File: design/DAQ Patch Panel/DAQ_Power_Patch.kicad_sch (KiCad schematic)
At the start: 18 parts, among them J1 Power 1 Terminal, J2 Screw_Terminal_01x06, J3 Power 2 Terminal, J4 12-Pole-PCB-Triple-Layer-Conn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, J7 Sensor 1 Terminal

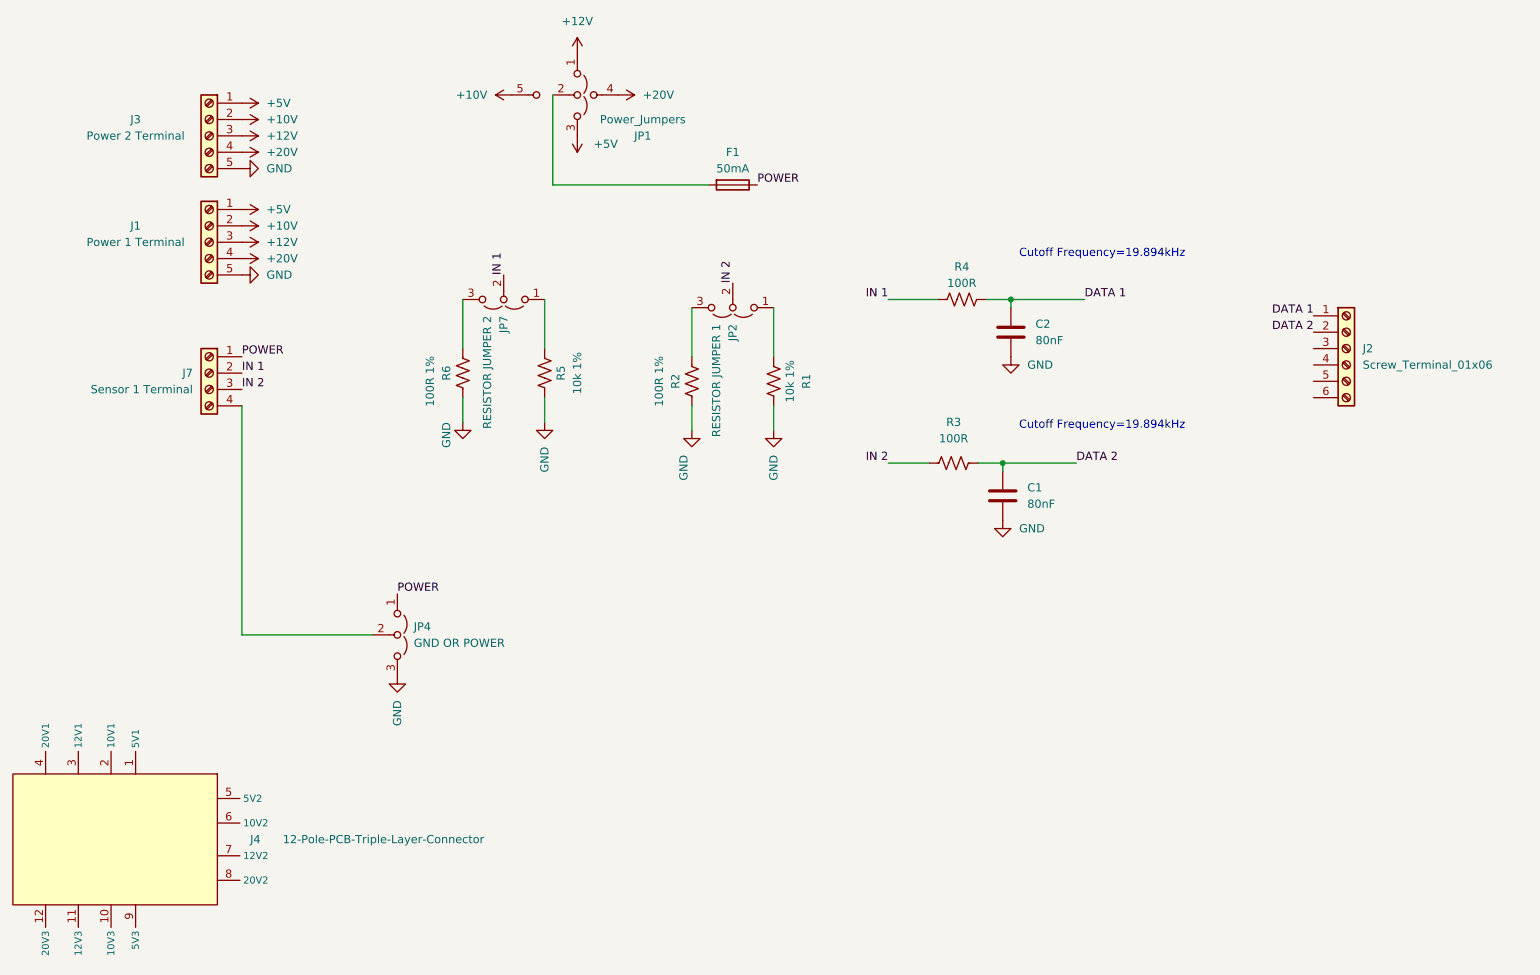
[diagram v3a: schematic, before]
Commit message: Hierarchecal Sheets Added and Sensor Ports Triplicated
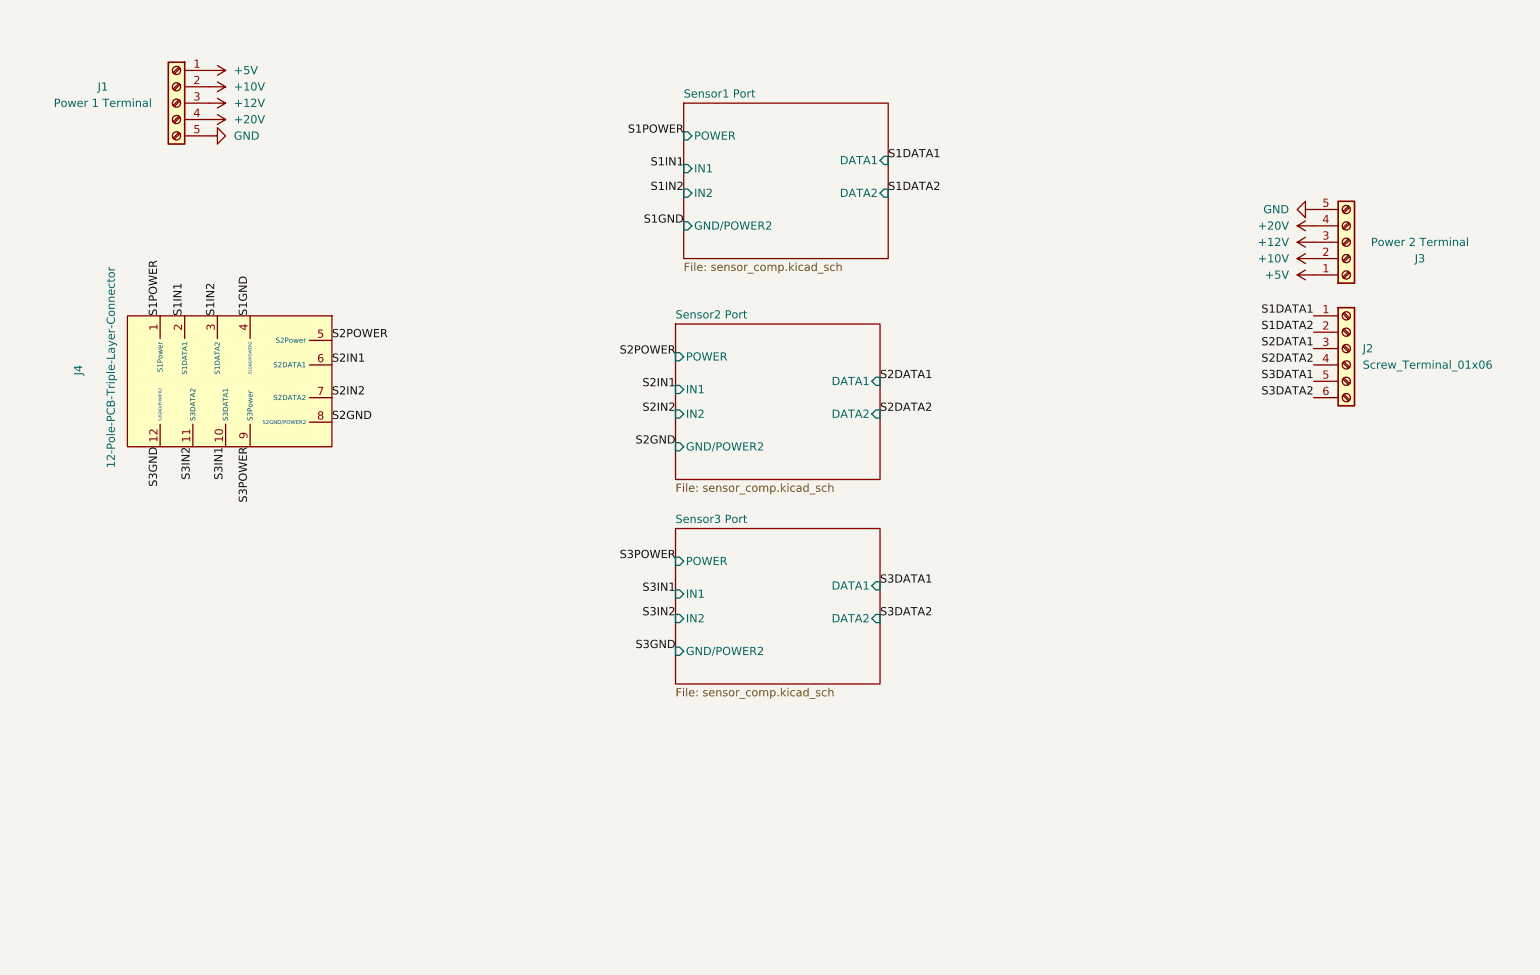
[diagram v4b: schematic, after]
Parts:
- removed C1, C2: 80nF, Capacitor_SMD:C_0805_2012Metric_Pad1.18x1.45mm_HandSolder, symbol Device:C
- removed F1: 50mA, Fuse:Fuse_0805_2012Metric_Pad1.15x1.40mm_HandSolder, symbol Device:Fuse
- removed J7: Sensor 1 Terminal, TerminalBlock_Phoenix:TerminalBlock_Phoenix_MKDS-1,5-4-5.08_1x04_P5.08mm_Horizontal, symbol Connector:Screw_Terminal_01x04
- removed JP1: Power_Jumpers, Library:4-Pole Jumper, symbol Jumper:Jumper_3_Open
- removed JP2: RESISTOR JUMPER 1, Connector_PinHeader_2.54mm:PinHeader_1x03_P2.54mm_Vertical, symbol Jumper:Jumper_3_Open
- removed JP4: GND OR POWER, Connector_PinHeader_2.54mm:PinHeader_1x03_P2.54mm_Vertical, symbol Jumper:Jumper_3_Open
- removed JP7: RESISTOR JUMPER 2, Connector_PinHeader_2.54mm:PinHeader_1x03_P2.54mm_Vertical, symbol Jumper:Jumper_3_Open
- removed R1, R5: 10k 1%, Resistor_SMD:R_0805_2012Metric_Pad1.20x1.40mm_HandSolder, symbol Device:R_US
- removed R2, R6: 100R 1%, Resistor_SMD:R_0805_2012Metric_Pad1.20x1.40mm_HandSolder, symbol Device:R_US
- removed R3, R4: 100R, Resistor_SMD:R_0805_2012Metric_Pad1.20x1.40mm_HandSolder, symbol Device:R_US
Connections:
- net S2DATA1: now reaches J2.3 (Pin_3)
- net S2DATA2: now reaches J2.4 (Pin_4)
- net S3DATA1: now reaches J2.5 (Pin_5)
- net S3DATA2: now reaches J2.6 (Pin_6)
- net S1POWER: now reaches J4.1 (S1Power)
- net S3IN1: now reaches J4.10 (S3DATA1)
- net S3IN2: now reaches J4.11 (S3DATA2)
- net S3GND: now reaches J4.12 (S3GND/POWER2)
- net S1IN1: now reaches J4.2 (S1DATA1)
- net S1IN2: now reaches J4.3 (S1DATA2)
- net S1GND: now reaches J4.4 (S1GND/POWER2)
- net S2POWER: now reaches J4.5 (S2Power)
- net S2IN1: now reaches J4.6 (S2DATA1)
- net S2IN2: now reaches J4.7 (S2DATA2)
- net S2GND: now reaches J4.8 (S2GND/POWER2)
- net S3POWER: now reaches J4.9 (S3Power)
- net DATA 1 renamed S1DATA1
- net DATA 2 renamed S1DATA2
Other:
- added sheet Sensor1 Port (sensor_comp.kicad_sch)
- added sheet Sensor2 Port (sensor_comp.kicad_sch)
- added sheet Sensor3 Port (sensor_comp.kicad_sch)
- note removed: "Cutoff Frequency=19.894kHz"
- moved on the sheet: J1, J3, J4

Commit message: Footprint and Hierarchal Sheets
Footprint for 6 screw terminal block added and sensor components made into hierarchical sheets
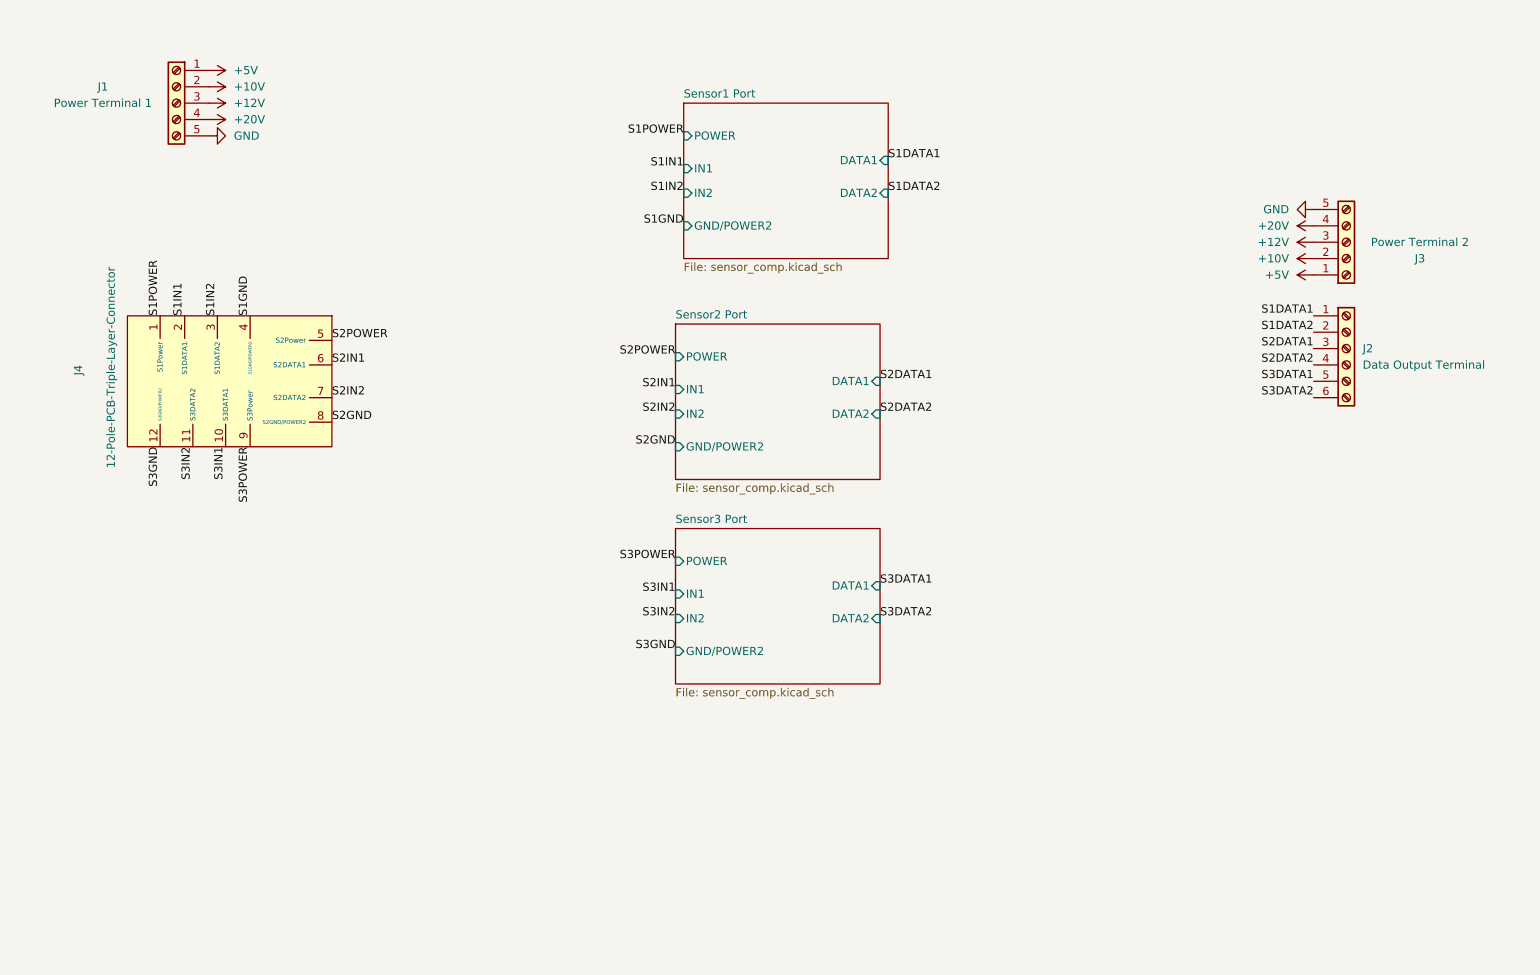
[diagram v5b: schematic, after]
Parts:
- J1: value Power 1 Terminal -> Power Terminal 1
- J2: value Screw_Terminal_01x06 -> Data Output Terminal; footprint (none) -> Library:TerminalBlock_Phoenix_MKDS_1,5-6-5-5.08_1x06P5.08
- J3: value Power 2 Terminal -> Power Terminal 2
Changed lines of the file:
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@@
   (title_block
     (title "DAQ_PATCH_PANEL")
-    (date "2023-11-13")
-    (rev "V-5")
+    (date "2023-12-16")
+    (rev "V-6")
     (company "Waterloo Rocketry ")
-    (comment 1 "Schematic to be triplicated for a total of 3 sensor ports per patch board")
   )
   (label "S2DATA2" (at 238.76 91.44 180) (fields_autoplaced)
@@
       (effects (font (size 1.27 1.27)) (justify left))
     )
-    (property "Value" "Screw_Terminal_01x06" (at 246.38 91.44 0)
-      (effects (font (size 1.27 1.27)) (justify left))
-    )
-    (property "Footprint" "" (at 243.84 88.9 0)
+    (property "Value" "Data Output Terminal" (at 246.38 91.44 0)
+      (effects (font (size 1.27 1.27)) (justify left))
+    )
+    (property "Footprint" "Library:TerminalBlock_Phoenix_MKDS_1,5-6-5-5.08_1x06P5.08" (at 243.84 88.9 0)
       (effects (font (size 1.27 1.27)) hide)
     )
@@
       (effects (font (size 1.27 1.27)))
     )
-    (property "Value" "Power 1 Terminal" (at 50.8 50.8 0)
+    (property "Value" "Power Terminal 1" (at 50.8 50.8 0)
       (effects (font (size 1.27 1.27)))
     )
@@
       (effects (font (size 1.27 1.27)))
     )
-    (property "Value" "Power 2 Terminal" (at 255.27 72.39 0)
+    (property "Value" "Power Terminal 2" (at 255.27 72.39 0)
       (effects (font (size 1.27 1.27)))
     )
